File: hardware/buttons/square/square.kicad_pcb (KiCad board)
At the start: 2 copper layers, 24.5 x 26.3 mm, 10 parts, among them J1 Conn_01x03, J2 Conn_01x03

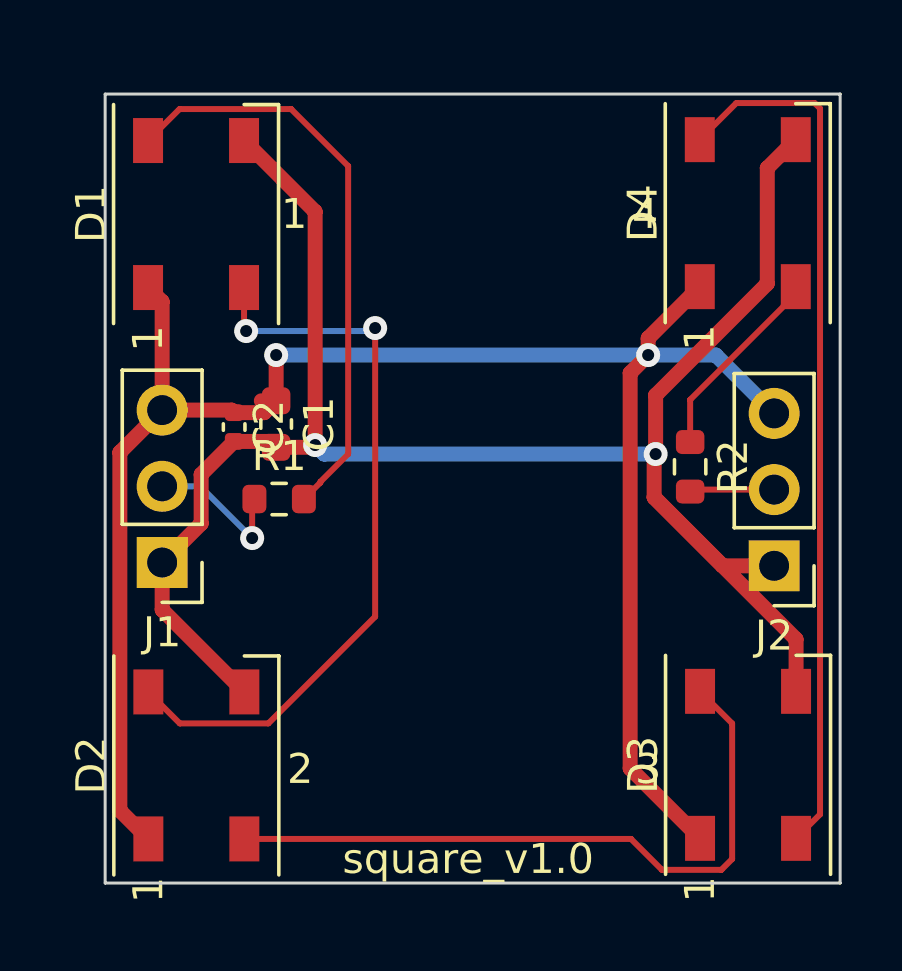
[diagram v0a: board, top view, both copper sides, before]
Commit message: Add mounting holes
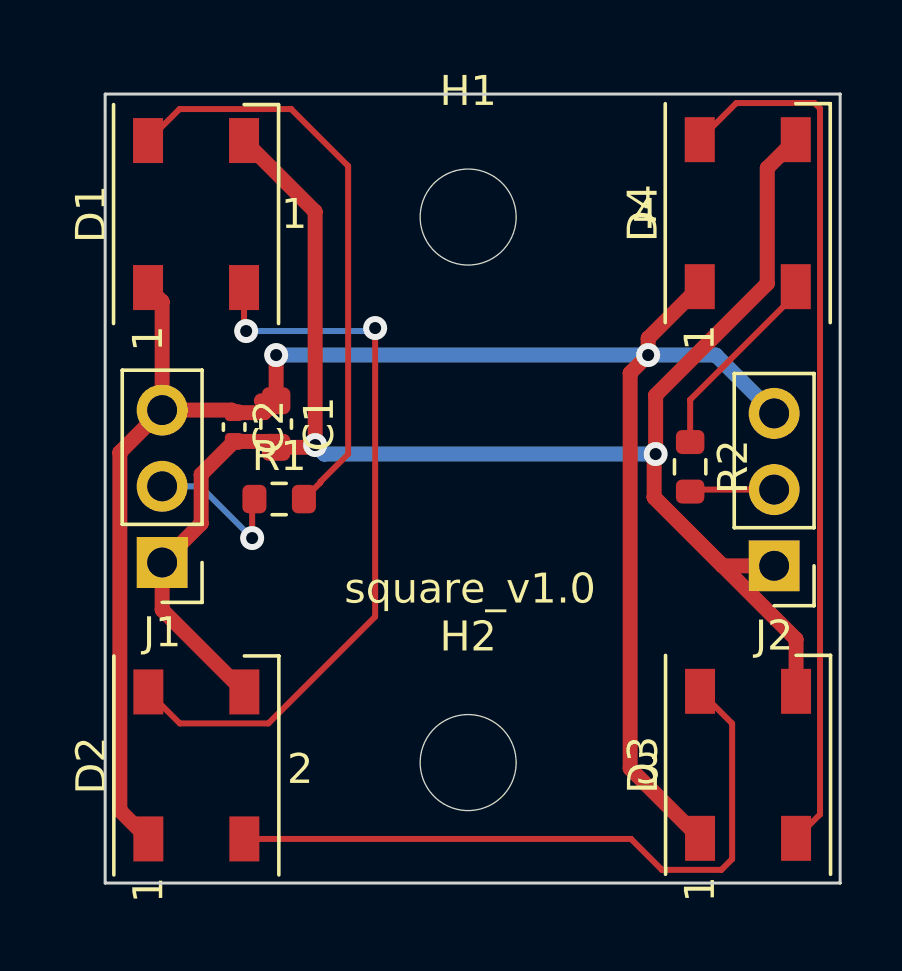
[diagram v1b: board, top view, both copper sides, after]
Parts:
- added H1: MountingHole, MountingHole:MountingHole_3.2mm_M3, F.Cu at (50.1, 36.7)
- added H2: MountingHole, MountingHole:MountingHole_3.2mm_M3, F.Cu at (50.1, 54.9)
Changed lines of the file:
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@@
     )
+  )
+  (footprint "MountingHole:MountingHole_3.2mm_M3" (layer "F.Cu")
+    (at 50.1 36.7)
+    (descr "Mounting Hole 3.2mm, no annular, M3")
+    (tags "mounting hole 3.2mm no annular m3")
+    (property "Sheetfile" "square.kicad_sch")
+    (property "Sheetname" "")
+    (attr exclude_from_pos_files)
+    (fp_text reference "H1" (at 0 -4.2) (layer "F.SilkS")
+      (effects (font (size 1 1) (thickness 0.15)))
+    )
+    (fp_text value "MountingHole" (at 0 4.2) (layer "F.Fab")
+      (effects (font (size 1 1) (thickness 0.15)))
+    )
+    (fp_text user "${REFERENCE}" (at 0 0) (layer "F.Fab")
+      (effects (font (size 1 1) (thickness 0.15)))
+    )
+    (fp_circle (center 0 0) (end 3.2 0) (layer "Cmts.User") (width 0.15) (fill none))
+    (fp_circle (center 0 0) (end 3.45 0) (layer "F.CrtYd") (width 0.05) (fill none))
+    (pad "" np_thru_hole circle (at 0 0) (size 3.2 3.2) (drill 3.2) (layers *.Cu *.Mask))
+  )
+  (footprint "MountingHole:MountingHole_3.2mm_M3" (layer "F.Cu")
+    (at 50.1 54.884117)
+    (descr "Mounting Hole 3.2mm, no annular, M3")
+    (tags "mounting hole 3.2mm no annular m3")
+    (property "Sheetfile" "square.kicad_sch")
+    (property "Sheetname" "")
+    (attr exclude_from_pos_files)
+    (fp_text reference "H2" (at 0 -4.2) (layer "F.SilkS")
+      (effects (font (size 1 1) (thickness 0.15)))
+    )
+    (fp_text value "MountingHole" (at 0 4.2) (layer "F.Fab")
+      (effects (font (size 1 1) (thickness 0.15)))
+    )
+    (fp_text user "${REFERENCE}" (at 0 0) (layer "F.Fab")
+      (effects (font (size 1 1) (thickness 0.15)))
+    )
+    (fp_circle (center 0 0) (end 3.2 0) (layer "Cmts.User") (width 0.15) (fill none))
+    (fp_circle (center 0 0) (end 3.45 0) (layer "F.CrtYd") (width 0.05) (fill none))
+    (pad "" np_thru_hole circle (at 0 0) (size 3.2 3.2) (drill 3.2) (layers *.Cu *.Mask))
   )
   (footprint "LED_SMD:LED_WS2812B_PLCC4_5.0x5.0mm_P3.2mm" (layer "F.Cu")
@@
     (effects (font (size 1 1) (thickness 0.15)))
   )
-  (gr_text "square_v1.0" (at 50.1 58.1) (layer "F.SilkS")
+  (gr_text "square_v1.0" (at 50.162971 49.087734) (layer "F.SilkS")
     (effects (font (size 1 1) (thickness 0.15)))
   )
